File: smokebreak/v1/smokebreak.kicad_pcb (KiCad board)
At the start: 6 copper layers, 94 x 52 mm, 208 parts, among them J1 XT60 male, J2 XT30 male, J3 XT60 female, J4 XT30 female, J5 JST-XH 9, J6 SWD, J7 TFT1901 FPC, J8 USB-C, Q1 input FET, Q10 BC817, Q11 BSC070N10LS5, Q2 output FET, Q3 SUD50P10-43L, Q4 MMBTA42, Q5 BC817, Q6 MMBT5401, Q7 MMBT5401, Q8 2N7002, Q9 AO3400A, SW1 ON-OFF-(ON), SW2 Limit -, SW3 Limit +, U1 TPS48000, U10 SN74AHCT1G125, U11 USBLC6-2SC6, U12 LMV331, U2 INA181A2, U3 LMR36506R5, U4 TLV75533, U5 STM32G0B1RBT6, U6 DRV5032FA, U7 74LVC1G11, U8 LMV331, U9 SN74LVC1G74

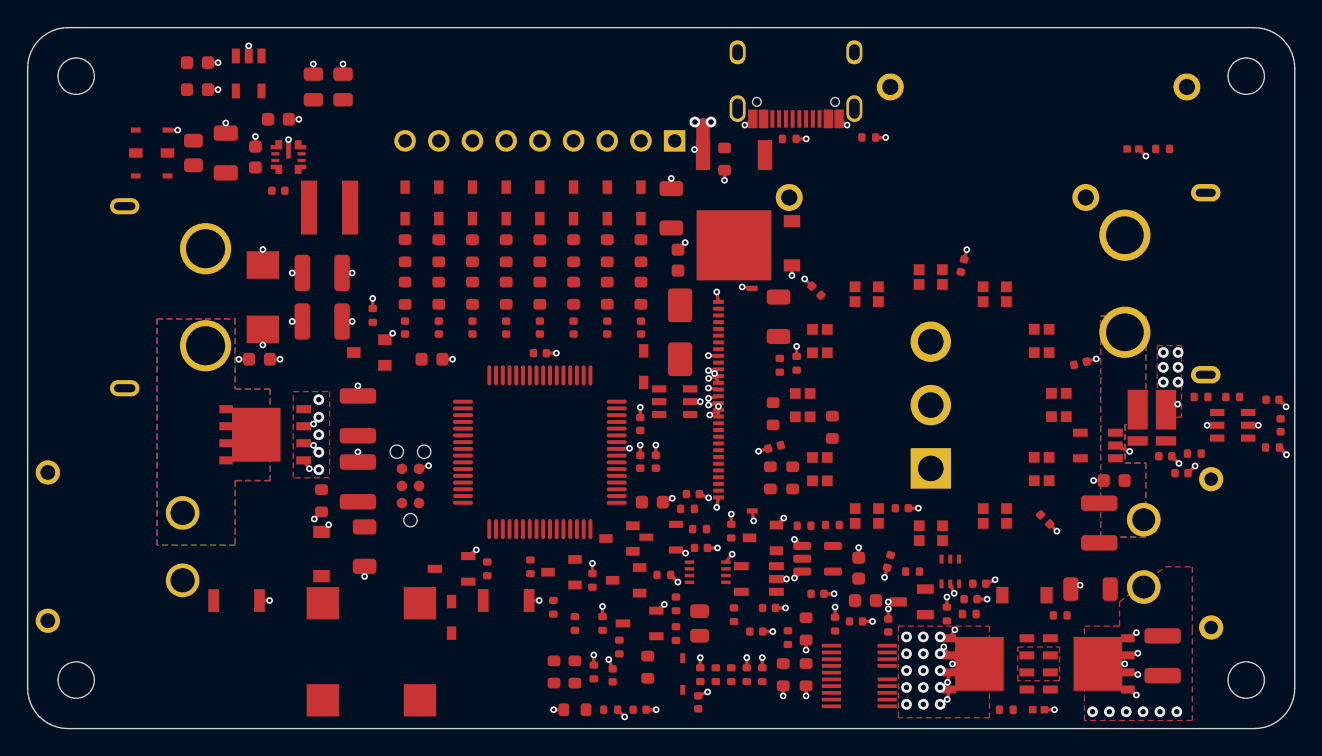
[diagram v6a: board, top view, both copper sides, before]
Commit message: smokebreak v1: 5 mil default class, repair stage (drop shorts/danglers, re-finish); current routed board (13 open)
Co-Authored-By: Claude Opus 5.5 <noreply@anthropic.com>
Claude-Session: https://claude.ai/code/session_01SBnFJLvm1wBa1jZy4RXnma
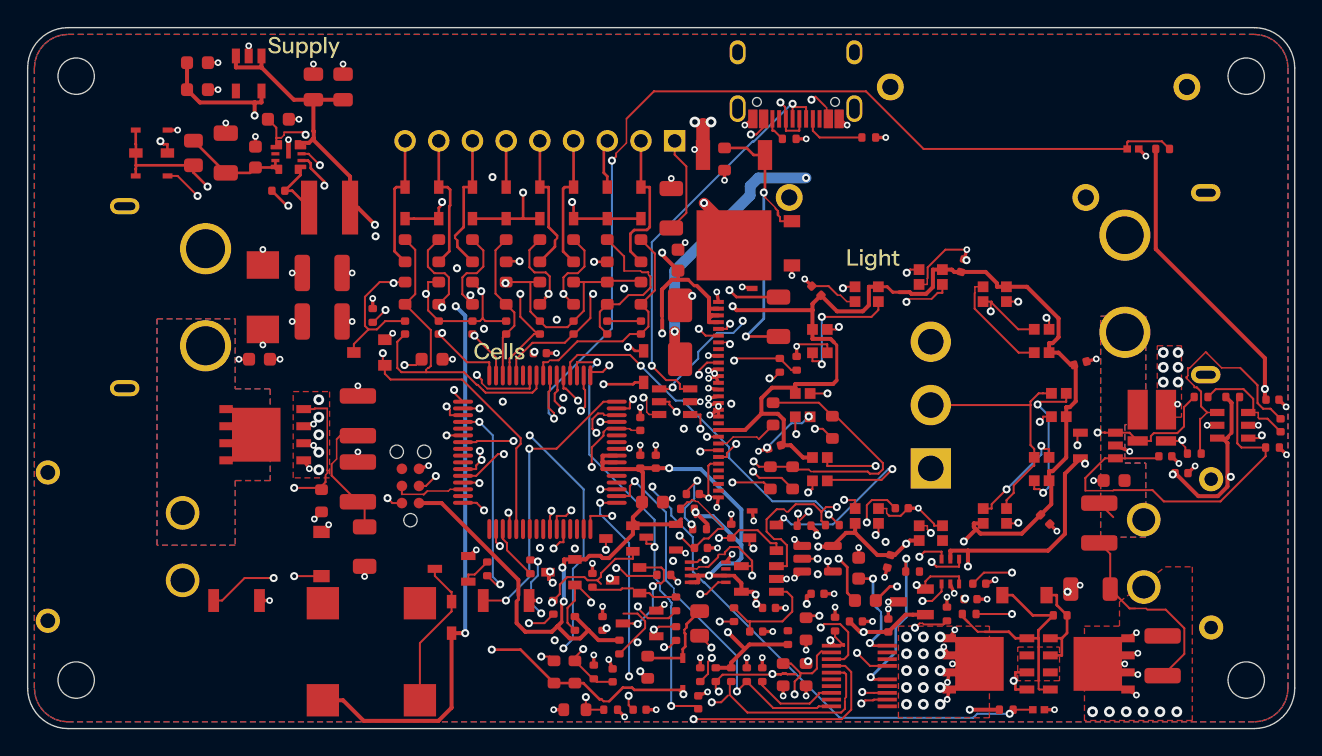
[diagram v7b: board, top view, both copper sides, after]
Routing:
- net +3V3: track 0.00 -> 280.1 mm, vias 0 -> 21
- net +5V: track 0.00 -> 194.4 mm, vias 0 -> 8
- net VOUT: track 6.50 -> 118.4 mm, vias 13 -> 18
- net VBUS: track 0.00 -> 92.6 mm, vias 0 -> 7
- net NTC_PRE: track 0.00 -> 71.8 mm, vias 0 -> 2
- net GND: track 78.5 -> 145.6 mm, vias 114 -> 119
- net AUX: track 0.00 -> 54.8 mm, vias 0 -> 4
- net TPS_FLTGD: track 0.00 -> 53.9 mm, vias 0 -> 5
- net USB_DM: track 0.00 -> 51.3 mm, vias 0 -> 5
- net TOG_ON: track 0.00 -> 49.1 mm, vias 0 -> 2
- net NTC_FET: track 0.00 -> 48.5 mm, vias 0 -> 3
- net GUARD_OPEN: track 0.00 -> 47.9 mm, vias 0 -> 4
- net I_SENSE: track 0.00 -> 47.6 mm, vias 0 -> 2
- net DIV_GND: track 0.00 -> 47.4 mm, vias 0 -> 4
- net VOUT_LO: track 0.00 -> 46.7 mm, vias 0 -> 4
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- added copper zone on B.Cu, net GND
- added copper zone on In2.Cu, net GND
- added copper zone on In3.Cu, net GND

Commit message: smokebreak v1: placer keeps parts off the power copper, hard-short comparator beside the FETs, thermistor at Q1, keep-outs become DRC rules in the final board
Co-Authored-By: Claude Opus 5.5 <noreply@anthropic.com>
Claude-Session: https://claude.ai/code/session_01SBnFJLvm1wBa1jZy4RXnma
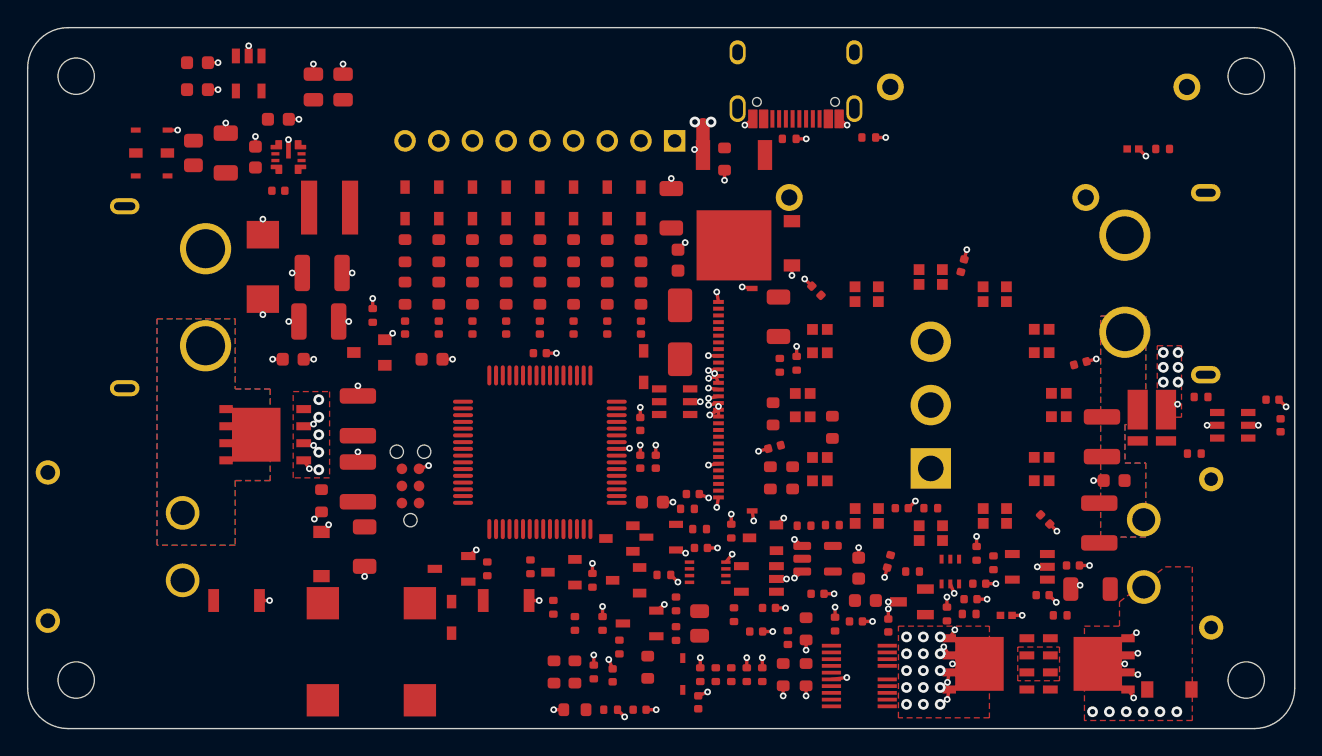
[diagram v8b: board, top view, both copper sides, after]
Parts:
- moved R71 23.3 mm to (170.4, 139.0), turned to 90 degrees
- moved R70 21.6 mm to (171.7, 139.7), turned to 90 degrees
- moved C52 16.9 mm to (179.7, 130.3)
- moved R35 16.0 mm to (167.0, 135.7)
- moved C55 13.7 mm to (175.3, 142.1)
- moved D18 12.8 mm to (184.7, 149.1)
- moved C56 10.6 mm to (177.6, 139.9)
- moved U12 10.3 mm to (174.3, 140.0)
- moved RT1 7.40 mm to (172.6, 143.6)
- moved C3 2.50 mm to (119.7, 124.6)
- moved D1 2.25 mm to (117.5, 117.8)
- moved C2 0.25 mm to (121.6, 121.8)
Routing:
- net +3V3: track 280.1 -> 0.00 mm, vias 21 -> 0
- net +5V: track 194.4 -> 0.00 mm, vias 8 -> 0
- net VOUT: track 118.4 -> 6.50 mm, vias 18 -> 13
- net VBUS: track 92.6 -> 0.00 mm, vias 7 -> 0
- net NTC_PRE: track 71.8 -> 0.00 mm, vias 2 -> 0
- net GND: track 145.6 -> 80.0 mm, vias 119 -> 116
- net AUX: track 54.8 -> 0.00 mm, vias 4 -> 0
- net TPS_FLTGD: track 53.9 -> 0.00 mm, vias 5 -> 0
- net USB_DM: track 51.3 -> 0.00 mm, vias 5 -> 0
- net TOG_ON: track 49.1 -> 0.00 mm, vias 2 -> 0
- net NTC_FET: track 48.5 -> 0.00 mm, vias 3 -> 0
- net GUARD_OPEN: track 47.9 -> 0.00 mm, vias 4 -> 0
- net I_SENSE: track 47.6 -> 0.00 mm, vias 2 -> 0
- net DIV_GND: track 47.4 -> 0.00 mm, vias 4 -> 0
- net VOUT_LO: track 46.7 -> 0.00 mm, vias 4 -> 0
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- removed copper zone on B.Cu, net GND
- removed copper zone on In2.Cu, net GND
- removed copper zone on In3.Cu, net GND
